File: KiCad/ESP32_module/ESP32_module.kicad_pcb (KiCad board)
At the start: 2 copper layers, 40 x 40 mm, 39 parts, among them J1 Conn_01x05_Pin, J2 Conn_01x05_Pin, J3 Conn_01x05_Pin, J4 Conn_01x05_Pin, J5 Conn_01x02_Pin, J6 Conn_01x02_Pin, J7 Conn_01x02_Pin, J8 Conn_01x02_Pin, J9 Conn_01x02_Pin, M1 ESP32_XAIO

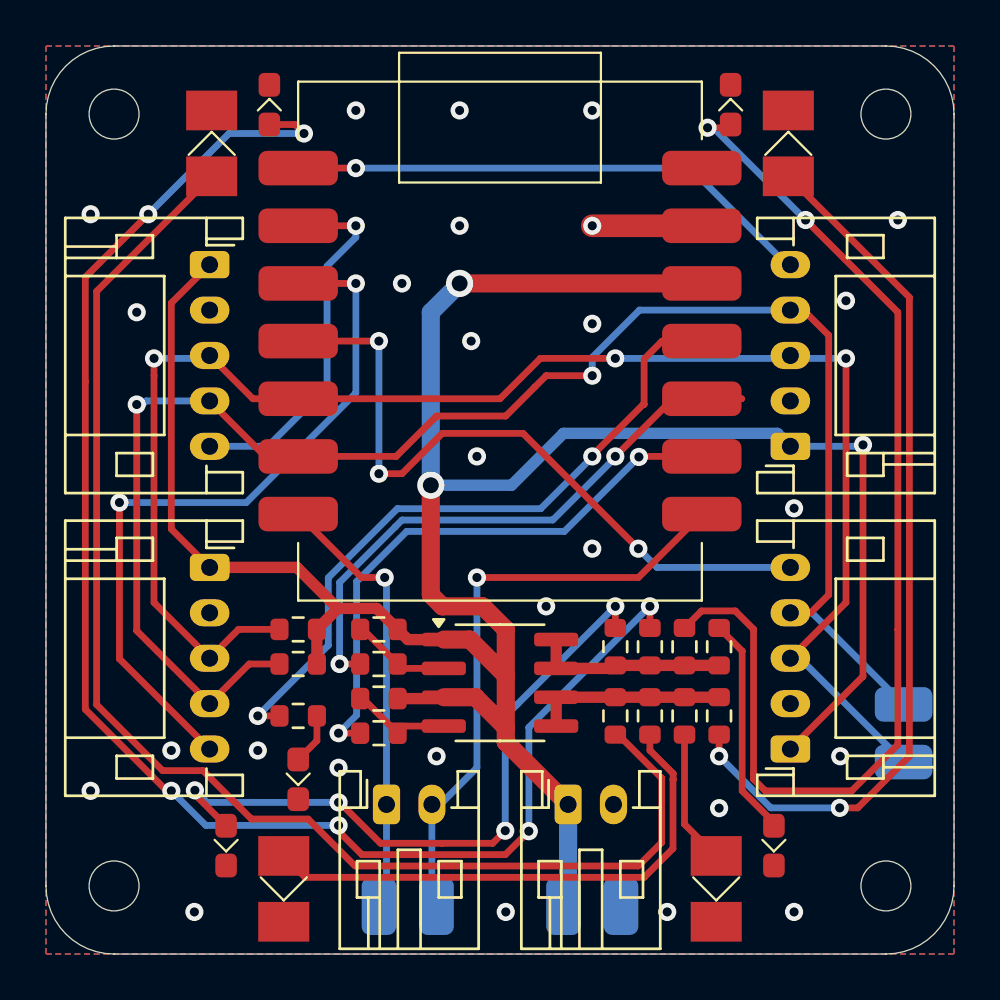
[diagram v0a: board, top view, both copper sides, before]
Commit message: fix mosfet
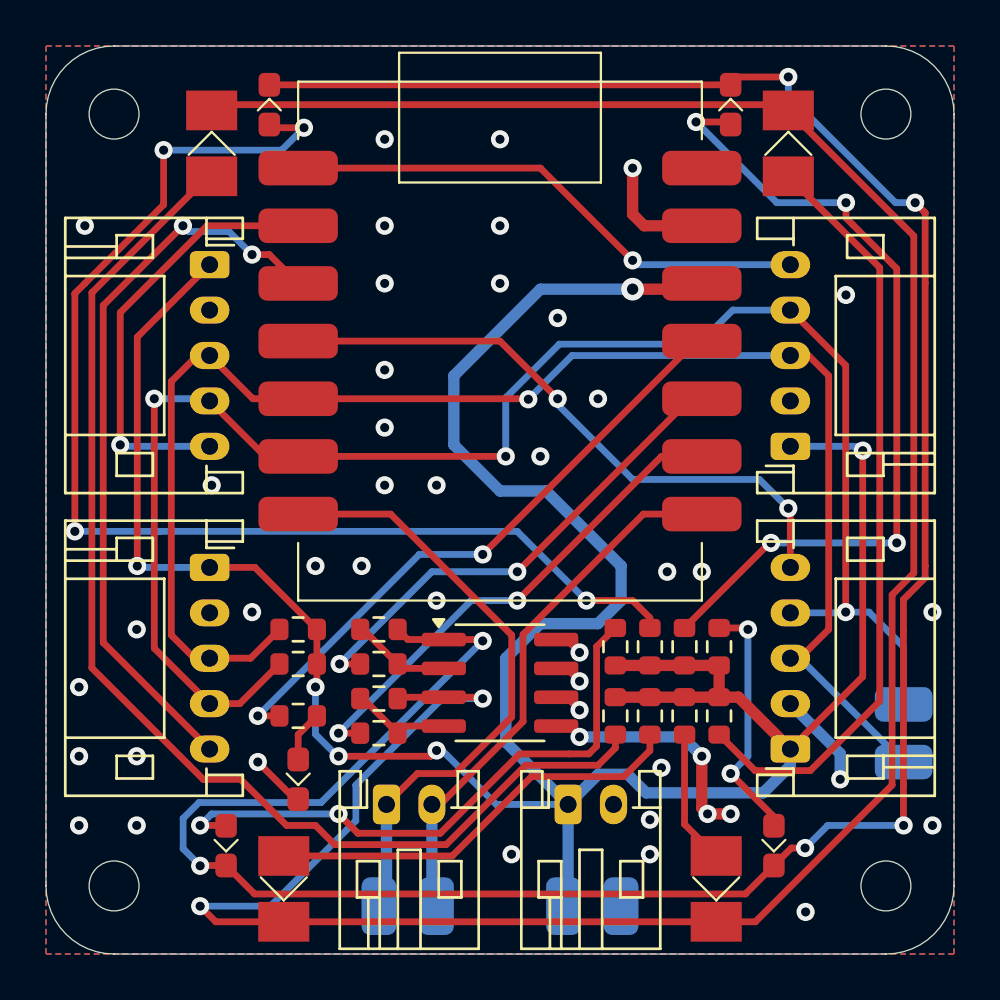
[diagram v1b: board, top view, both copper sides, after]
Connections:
- D2 pad 1: GND1 -> Net-(D2-K)
- D3 pad 1: GND1 -> Net-(D2-K)
- D4 pad 1: GND1 -> Net-(D2-K)
- D5 pad 1: GND1 -> Net-(D2-K)
- D6 pad 1: GND1 -> Net-(D6-K)
- D7 pad 1: GND1 -> Net-(D6-K)
- D8 pad 1: GND1 -> Net-(D6-K)
- D9 pad 1: GND1 -> Net-(D6-K)
- FET1 pad 1: +3.3V -> Net-(D6-K)
- FET1 pad 3: +3.3V -> Net-(D2-K)
- FET1 pad 5: Net-(FET1-Drain_2-Pad5) -> GND1
- FET1 pad 6: Net-(FET1-Drain_2-Pad5) -> GND1
- FET1 pad 7: Net-(FET1-Drain_1-Pad7) -> GND1
- FET1 pad 8: Net-(FET1-Drain_1-Pad7) -> GND1
- R10 pad 1: Net-(FET1-Drain_2-Pad5) -> +3.3V
- R11 pad 1: Net-(FET1-Drain_2-Pad5) -> +3.3V
- R12 pad 1: Net-(FET1-Drain_1-Pad7) -> +3.3V
- R13 pad 1: Net-(FET1-Drain_1-Pad7) -> +3.3V
- R14 pad 1: Net-(FET1-Drain_1-Pad7) -> +3.3V
- R15 pad 1: Net-(FET1-Drain_1-Pad7) -> +3.3V
- R6 pad 2: +3.3V -> Net-(D6-K)
- R7 pad 2: +3.3V -> Net-(D2-K)
- R8 pad 1: Net-(FET1-Drain_2-Pad5) -> +3.3V
- R9 pad 1: Net-(FET1-Drain_2-Pad5) -> +3.3V
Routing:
- net Net-(D6-K): track 0.00 -> 114.9 mm, vias 0 -> 6
- net Net-(D2-K): track 0.00 -> 112.2 mm, vias 0 -> 2
- net GND1: track 4.83 -> 26.4 mm, vias 27 -> 45
- net +3.3V: track 115.1 -> 130.2 mm, vias 3 -> 6
- net Net-(D6-A): track 68.8 -> 53.9 mm, vias 6 -> 4
- net Net-(D7-A): track 49.6 -> 36.5 mm, vias 2 -> 4
- net Net-(FET1-Drain_1-Pad7): track 8.50 -> 0.00 mm
- net Net-(FET1-Drain_2-Pad5): track 8.45 -> 0.00 mm
- net TX: track 19.6 -> 27.0 mm, vias 1 -> 0
- net Net-(D2-A): track 59.3 -> 52.6 mm
- net Net-(M1-D9): track 27.3 -> 21.7 mm
- net Net-(D3-A): track 39.0 -> 33.8 mm, vias 2 -> 0
- net Net-(D4-A): track 23.5 -> 18.8 mm
- net Net-(D8-A): track 29.8 -> 26.3 mm, vias 4 -> 2
- net Net-(M1-D8): track 25.5 -> 22.0 mm
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
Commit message: fix gnd
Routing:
- net GND1: vias 45 -> 46
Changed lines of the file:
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@@
+	)
+	(via
+		(at 163.322 76.962)
+		(size 0.8)
+		(drill 0.4)
+		(layers "F.Cu" "B.Cu")
+		(free yes)
+		(net 2)
 	)
 	(via

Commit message: fix
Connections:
- FET1 pad 1: Net-(D6-K) -> GND1
- FET1 pad 3: Net-(D2-K) -> GND1
- FET1 pad 5: GND1 -> Net-(D2-K)
- FET1 pad 6: GND1 -> Net-(D2-K)
- FET1 pad 7: GND1 -> Net-(D6-K)
- FET1 pad 8: GND1 -> Net-(D6-K)
- R6 pad 2: Net-(D6-K) -> GND1
- R7 pad 2: Net-(D2-K) -> GND1
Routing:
- net GND1: track 26.4 -> 16.3 mm, vias 46 -> 40
- net +3.3V: track 130.2 -> 124.0 mm
- net Net-(D6-K): track 114.9 -> 119.0 mm
- net Net-(D2-K): track 112.2 -> 115.5 mm

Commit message: fix
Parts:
- added G***: LOGO, esp32_lib_pcb:SW_ICON, B.Cu at (188.3, 80.4)
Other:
- board text added: "ESP32_Module_V1"
